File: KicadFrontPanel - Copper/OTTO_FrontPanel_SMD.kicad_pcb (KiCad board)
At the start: 2 copper layers, 294.5 x 102.3 mm, 75 parts, among them SW1 ALPS SKHC, SW10 ALPS SKHC, SW11 ALPS SKHC, SW12 ALPS SKHC, SW13 ALPS SKHC, SW14 ALPS SKHC, SW15 ALPS SKHC, SW16 ALPS SKHC, SW17 ALPS SKHC, SW18 ALPS SKHC, SW19 ALPS SKHC, SW2 ALPS SKHC, SW20 ALPS SKHC, SW21 ALPS SKHC, SW22 ALPS SKHC, SW23 ALPS SKHC, SW24 ALPS SKHC, SW25 ALPS SKHC, SW26 ALPS SKHC, SW3 ALPS SKHC, SW32 6x6x13mm, SW33 6x6x13mm, SW38 6x6x13mm, SW4 ALPS SKHC, SW5 ALPS SKHC, SW6 ALPS SKHC, SW7 ALPS SKHC, SW8 ALPS SKHC, SW9 ALPS SKHC

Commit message: Added version to silkscreen on frontplates
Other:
- board text added: "v0.2.0 - COPPER"

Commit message: Hardware v0.2.0 as ordered
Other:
- board text added: "v0.2.0 - CUPPER"
- board text removed: "v0.2.0 - COPPER"

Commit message: Frontpanel changes
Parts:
- moved G*** 5.03 mm to (35.1, 27.1)
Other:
- outline, holes or cut-outs redrawn
- board text added: "v0.3.0 - COPPER"
- board text removed: "v0.2.0 - CUPPER"

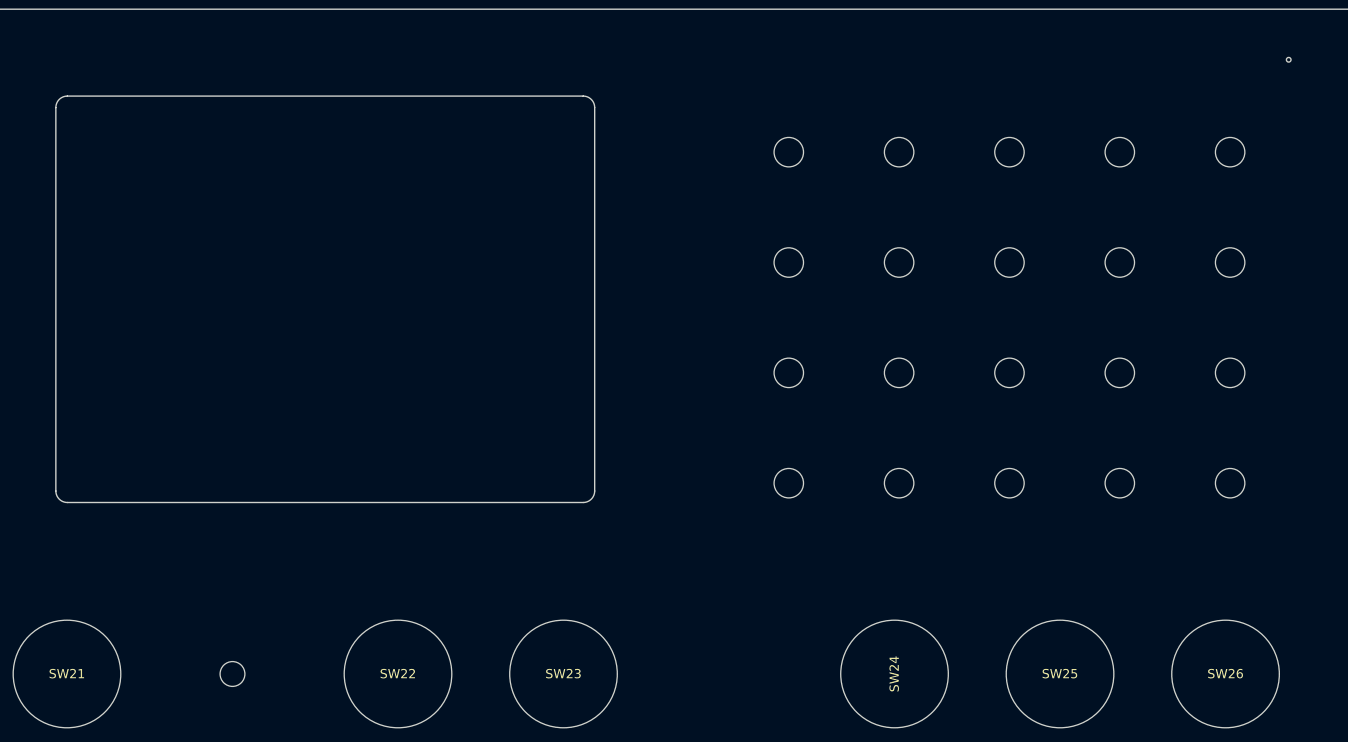
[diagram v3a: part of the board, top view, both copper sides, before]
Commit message: AUX: kbd key cutouts, screen cutout, H1-H5. Front plate: remove screw hole, mic rings footprint
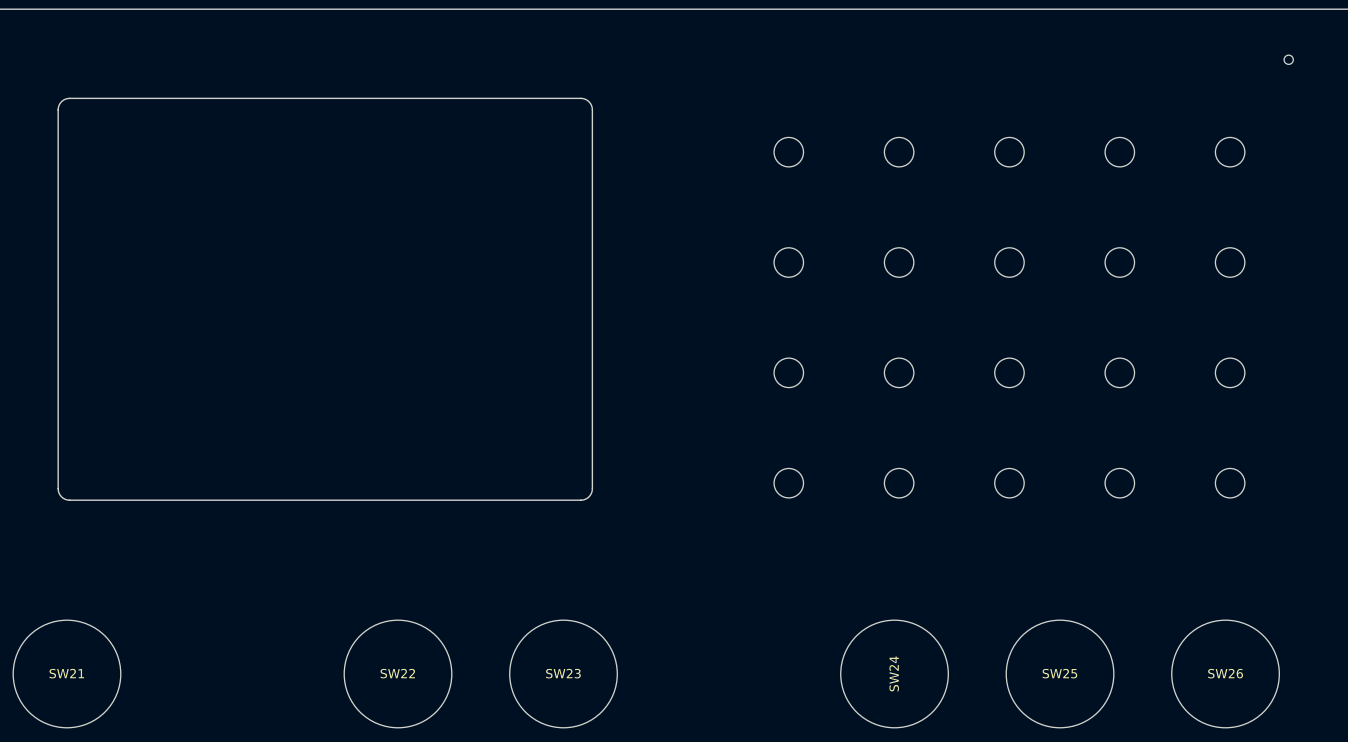
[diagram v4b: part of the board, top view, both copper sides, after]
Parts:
- removed ?: MountingHole_2.7mm_M2.5, MountingHole:MountingHole_2.7mm_M2.5
- added REF**: mic_hole_front_plate, OTTO_Footprints_Lib:mic_hole_front_plate, F.Cu at (276.1, 13.8)
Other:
- outline, holes or cut-outs redrawn
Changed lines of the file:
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@@
   (general
     (thickness 1.6)
-    (drawings 46)
+    (drawings 42)
     (tracks 0)
     (zones 0)
@@
     (diff_pair_gap 0.2032)
   )
+  (module OTTO_Footprints_Lib:mic_hole_front_plate (layer F.Cu)
+    (at 276.07 13.8)
+    (fp_text reference REF** (at 0 2.9718) (layer F.SilkS) hide
+      (effects (font (size 1 1) (thickness 0.15)))
+    )
+    (fp_text value mic_hole_front_plate (at 0 -3.9116) (layer F.Fab)
+      (effects (font (size 1 1) (thickness 0.15)))
+    )
+    (fp_circle (center 0 0) (end 2.2 0) (layer F.Mask) (width 0.12))
+    (fp_circle (center 0 0) (end 1.5 0) (layer F.Mask) (width 0.12))
+    (fp_circle (center 0 0) (end 0.8 0) (layer F.Mask) (width 0.12))
+    (pad "" np_thru_hole circle (at 0 0) (size 1 1) (drill 1) (layers *.Cu *.Mask))
+  )
   (module OTTO_Footprints_Lib:ALPS_SKHC (layer F.Cu)
     (at 134.2 96.1)
@@
       (xy -0.355563 -0.448924) (xy -0.137591 -0.585654) (xy 0.122575 -0.608498) (xy 0.33756 -0.548727)) (layer F.Mask) (width 0.01))
   )
-  (module MountingHole:MountingHole_2.7mm_M2.5 (layer F.Cu)
-    (at 161.2 80.6)
-    (descr "Mounting Hole 2.7mm, no annular, M2.5")
-    (tags "mounting hole 2.7mm no annular m2.5")
-    (attr virtual)
-    (fp_text reference "" (at 0 -3.7) (layer F.SilkS) hide
-      (effects (font (size 1 1) (thickness 0.15)))
-    )
-    (fp_text value MountingHole_2.7mm_M2.5 (at 0 3.7) (layer F.Fab)
-      (effects (font (size 1 1) (thickness 0.15)))
-    )
-    (fp_circle (center 0 0) (end 2.95 0) (layer F.CrtYd) (width 0.05))
-    (fp_circle (center 0 0) (end 2.7 0) (layer Cmts.User) (width 0.15))
-    (fp_text user %R (at 0.3 0) (layer F.Fab)
-      (effects (font (size 1 1) (thickness 0.15)))
-    )
-    (pad 1 np_thru_hole circle (at 0 0) (size 2.7 2.7) (drill 2.7) (layers *.Cu *.Mask))
-  )
   (module OTTO_Footprints_Lib:RightAngle_Small (layer B.Cu)
     (at 34.96 109.61)
@@
       (solder_mask_margin 1.5) (clearance 1.5))
   )
-  (gr_circle (center 276.07 13.8) (end 278.102 14.816) (layer F.Mask) (width 0.15))
-  (gr_circle (center 276.07 13.8) (end 277.34 14.562) (layer F.Mask) (width 0.15))
-  (gr_circle (center 276.07 13.8) (end 276.832 14.054) (layer F.Mask) (width 0.15))
   (gr_text "v0.3.0 - COPPER" (at 68.7336 107.0188) (layer B.SilkS)
     (effects (font (size 2 2) (thickness 0.25)) (justify mirror))
@@
   (gr_line (start 14.73 110.6) (end 307.67 110.6) (layer Edge.Cuts) (width 0.15))
   (target plus (at 0 145) (size 5) (width 0.15) (layer Edge.Cuts))
-  (gr_arc (start 199.34 60.7) (end 199.34 61.95) (angle -90) (layer Edge.Cuts) (width 0.15))
-  (gr_arc (start 143.241041 60.7) (end 141.991041 60.7) (angle -90) (layer Edge.Cuts) (width 0.15))
+  (gr_arc (start 199.09 60.45) (end 199.09 61.7) (angle -90) (layer Edge.Cuts) (width 0.15))
+  (gr_arc (start 143.491041 60.45) (end 142.241041 60.45) (angle -90) (layer Edge.Cuts) (width 0.15))
   (gr_line (start 23.7 85.5) (end 28.7 85.5) (layer F.Mask) (width 1))
-  (gr_circle (center 276.07 13.8) (end 276.32 13.8) (layer Edge.Cuts) (width 0.15))
   (gr_text JLCJLCJLCJLC (at 287.2 105.55) (layer B.SilkS)
     (effects (font (size 1 1) (thickness 0.15)) (justify mirror))
   )
-  (gr_arc (start 143.24 19) (end 143.24 17.75) (angle -90) (layer Edge.Cuts) (width 0.15))
-  (gr_arc (start 199.34 19) (end 200.59 19) (angle -90) (layer Edge.Cuts) (width 0.15))
-  (gr_line (start 143.24 17.75) (end 199.34 17.75) (layer Edge.Cuts) (width 0.15))
-  (gr_line (start 143.241041 61.95) (end 199.34 61.95) (layer Edge.Cuts) (width 0.15))
-  (gr_line (start 141.99 19) (end 141.991041 60.7) (layer Edge.Cuts) (width 0.15))
-  (gr_line (start 200.59 19) (end 200.59 60.7) (layer Edge.Cuts) (width 0.15))
+  (gr_arc (start 143.49 19.25) (end 143.49 18) (angle -90) (layer Edge.Cuts) (width 0.15))
+  (gr_arc (start 199.09 19.25) (end 200.34 19.25) (angle -90) (layer Edge.Cuts) (width 0.15))
+  (gr_line (start 143.49 18) (end 199.09 18) (layer Edge.Cuts) (width 0.15))
+  (gr_line (start 143.491041 61.7) (end 199.09 61.7) (layer Edge.Cuts) (width 0.15))
+  (gr_line (start 142.24 19.25) (end 142.241041 60.45) (layer Edge.Cuts) (width 0.15))
+  (gr_line (start 200.34 19.25) (end 200.34 60.45) (layer Edge.Cuts) (width 0.15))
   (target plus (at 0 114.3) (size 5) (width 0.15) (layer Edge.Cuts))
   (target plus (at 330.2 0) (size 5) (width 0.15) (layer Edge.Cuts))
